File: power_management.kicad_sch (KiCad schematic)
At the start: 21 parts, among them IC3 MCP73831T-2ATI_OT, IC4 AP2112K-3.3TRG1, J2 USB_C_Receptacle_USB2.0_14P, Q1 AO3401A

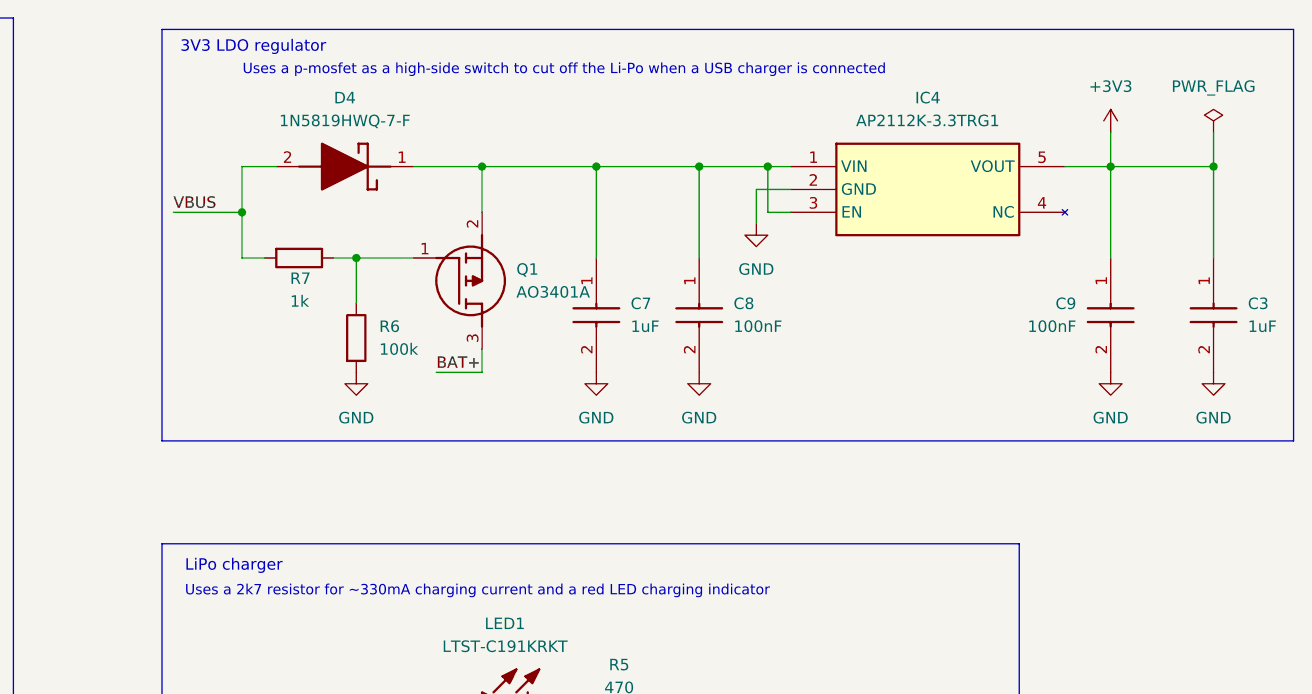
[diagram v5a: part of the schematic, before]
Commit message: added a ferride bead, added a 100nF filtering cap to the mosfet gate and changed the resistor pulldown value from 100k to 1k, removed the 1k resistor in series at the gate pin
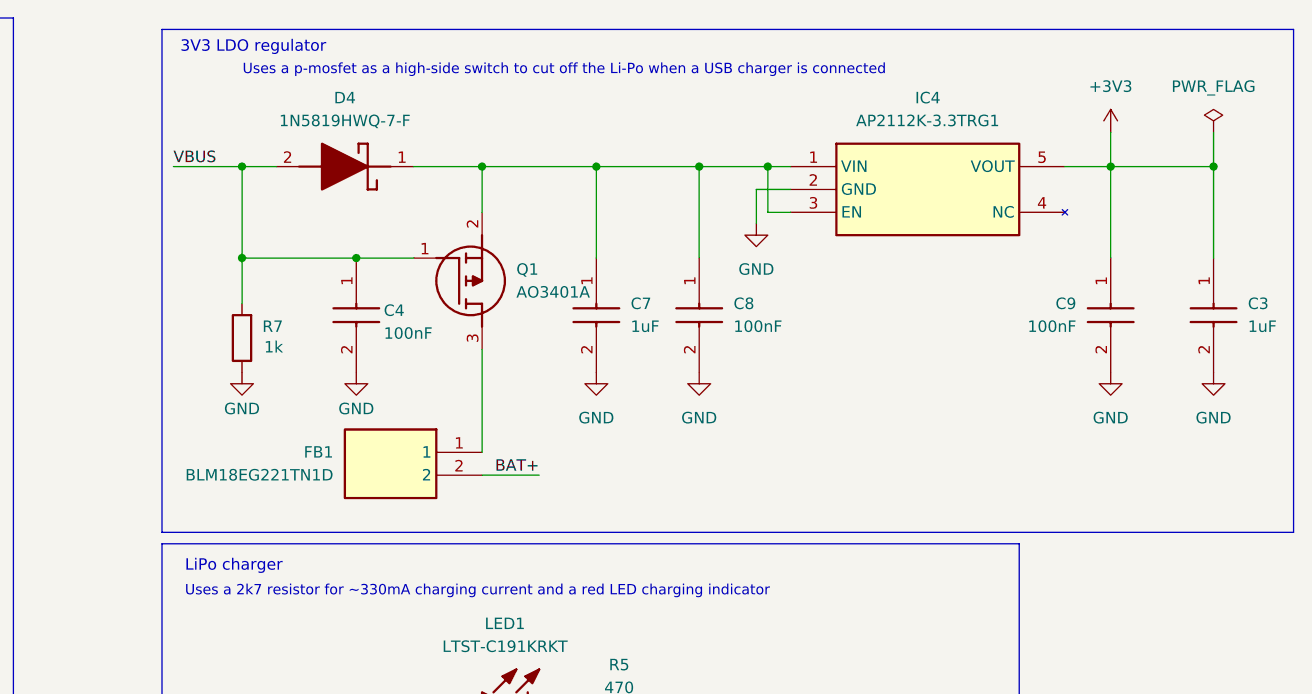
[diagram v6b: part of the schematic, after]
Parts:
- removed R6: 100k, Resistor_SMD:R_0603_1608Metric_Pad0.98x0.95mm_HandSolder, symbol Device:R
- added C4: 100nF, LifeCounter-Footprints:Kemet_C0603, symbol LifeCounter-Symbols:C0603C104K8RACTU
- added FB1: BLM18EG221TN1D, LifeCounter-Footprints:Murata_BLM18EG101TH1D, symbol LifeCounter-Symbols:BLM18EG221TN1D
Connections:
- net BAT+: now also FB1.2; no longer Q1.3 (D)
- net GND: now also R7.1, C4.2
- net VBUS: now also Q1.1 (G), C4.1
- new net: FB1.1, Q1.3 (D)
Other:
- moved on the sheet: R7
